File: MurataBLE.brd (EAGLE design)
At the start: 90 x 70 mm, 52 parts, among them IC1 I-5448, X1 TSW-114-02-S-S, X2 TSW-114-02-S-S

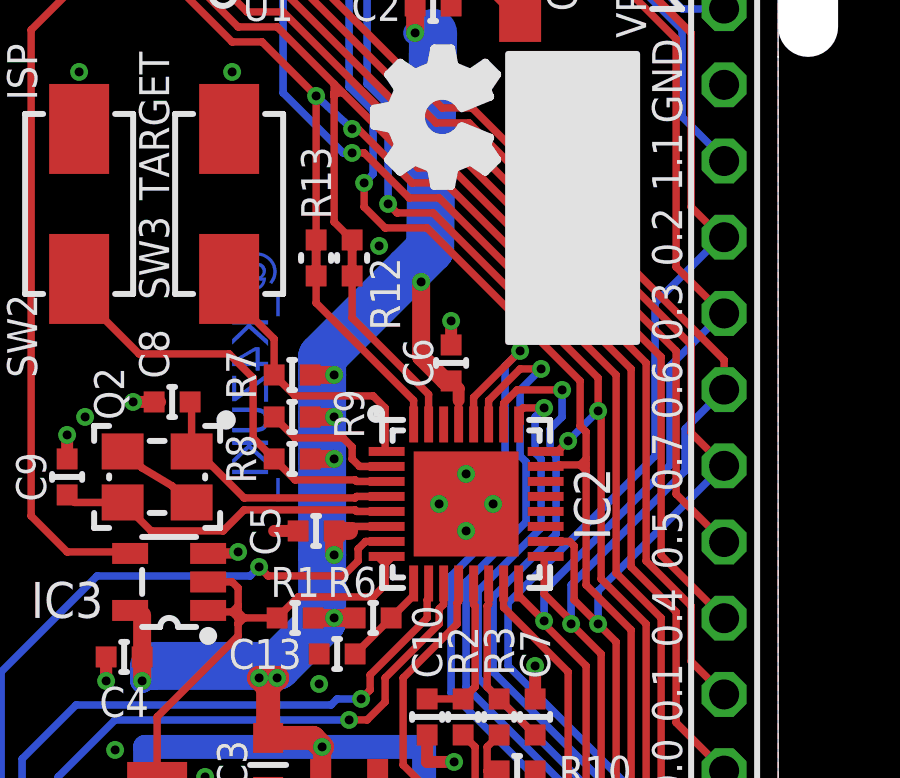
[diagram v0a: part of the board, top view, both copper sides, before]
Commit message: [ USB ] add SWD pulp R14/15
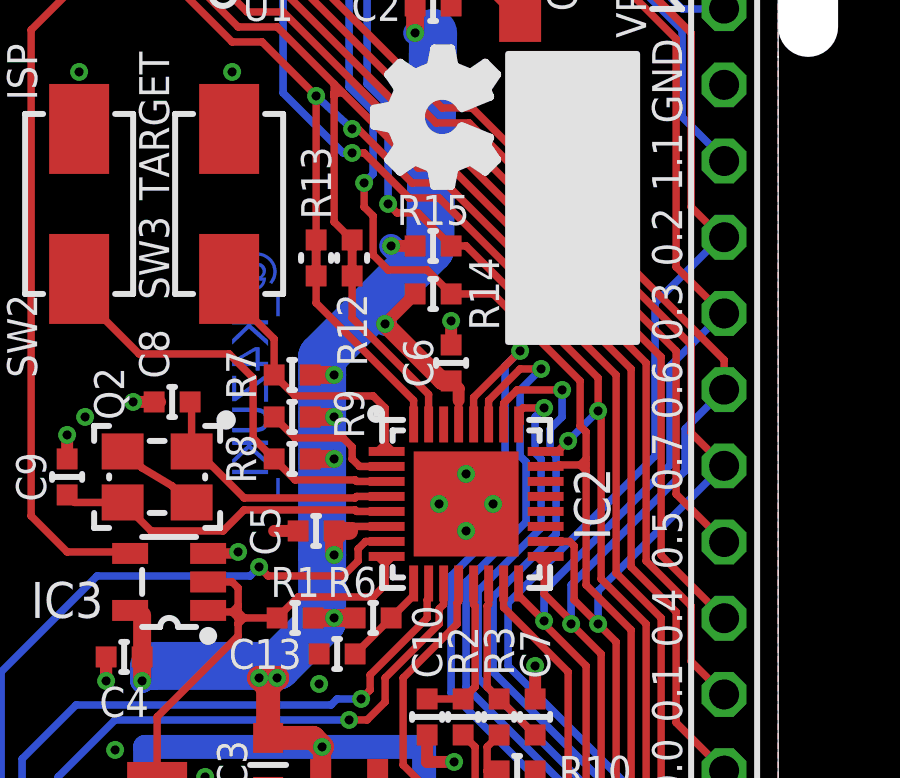
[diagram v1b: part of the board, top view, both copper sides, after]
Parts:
- added R14, R15: 10k/1005, mylib:C0402
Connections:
- net 3.3V: now also R14.2, R15.2
- net SWCLK: now also R14.1
- net SWDIO: now also R15.1
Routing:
- net 3.3V: track 96.3 -> 98.8 mm, vias 12 -> 13
- net SWCLK: track 42.9 -> 43.6 mm
- net FB_BL: track 9.45 -> 10.0 mm
- net 580.P0_6: track 52.0 -> 52.6 mm
- net GND: vias 71 -> 70
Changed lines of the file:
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@@
 <element name="R12" library="mylib" package="R0402SHORT" value="" x="24.8" y="43.2" smashed="yes" rot="R90">
 <attribute name="NOT_COMPONENT" value="YES" x="24.8" y="43.2" size="1.778" layer="27" rot="R90" display="off"/>
-<attribute name="NAME" x="25.9" y="42" size="1" layer="25" font="vector" ratio="20" rot="R90" align="center"/>
+<attribute name="NAME" x="24.8" y="40.8" size="1" layer="25" font="vector" ratio="20" rot="R90" align="center"/>
 <attribute name="VALUE" x="24.8" y="43.2" size="1" layer="27" font="vector" rot="R90" align="center"/>
 </element>
@@
 <attribute name="MOUSER" value="" x="11.8" y="35" size="1.778" layer="27" rot="R270" display="off"/>
 <attribute name="DIGIKEY" value="" x="11.8" y="35" size="1.778" layer="27" rot="R270" display="off"/>
+</element>
+<element name="R14" library="mylib" package="C0402" value="10k/1005" x="27.5" y="42" smashed="yes" rot="R180">
+<attribute name="MOUSER" value="" x="27.5" y="42" size="1.778" layer="27" rot="R180" display="off"/>
+<attribute name="AKIZUKI" value="" x="27.5" y="42" size="1.778" layer="27" rot="R180" display="off"/>
+<attribute name="DIGIKEY" value="P10.0KLCT-ND" x="27.5" y="42" size="1.778" layer="27" rot="R180" display="off"/>
+<attribute name="SEEED" value="301010047 " x="27.5" y="42" size="1.778" layer="27" rot="R180" display="off"/>
+<attribute name="NAME" x="29.2" y="42" size="1" layer="25" font="vector" ratio="20" rot="R270" align="center"/>
+<attribute name="VALUE" x="27.5" y="42" size="1" layer="27" font="vector" rot="R180" align="center"/>
+</element>
+<element name="R15" library="mylib" package="C0402" value="10k/1005" x="27.5" y="43.6" smashed="yes" rot="R180">
+<attribute name="MOUSER" value="" x="27.5" y="43.6" size="1.778" layer="27" rot="R180" display="off"/>
+<attribute name="AKIZUKI" value="" x="27.5" y="43.6" size="1.778" layer="27" rot="R180" display="off"/>
+<attribute name="DIGIKEY" value="P10.0KLCT-ND" x="27.5" y="43.6" size="1.778" layer="27" rot="R180" display="off"/>
+<attribute name="SEEED" value="301010047 " x="27.5" y="43.6" size="1.778" layer="27" rot="R180" display="off"/>
+<attribute name="NAME" x="27.5" y="44.8" size="1" layer="25" font="vector" ratio="20" rot="R180" align="center"/>
+<attribute name="VALUE" x="27.5" y="43.6" size="1" layer="27" font="vector" rot="R180" align="center"/>
 </element>
 </elements>
@@
 <contactref element="IC2" pad="EXP"/>
 <wire x1="29.5" y1="35" x2="28.6" y2="35" width="0.25" layer="1"/>
-<via x="25.7" y="43.6" extent="1-16" drill="0.3" diameter="0.45"/>
 <contactref element="C11" pad="2"/>
 <contactref element="C12" pad="2"/>
@@
 <wire x1="23.8" y1="37.9" x2="24.2" y2="37.9" width="0.8" layer="16"/>
 <wire x1="27.4" y1="43.5" x2="27.5" y2="50.7" width="1.6" layer="16"/>
-<wire x1="28.1" y1="39.1" x2="27.9" y2="39.1" width="0.6" layer="1"/>
-<wire x1="27.9" y1="39.1" x2="27.1" y2="39.9" width="0.6" layer="1"/>
+<wire x1="28.1" y1="39.1" x2="27.8" y2="39.1" width="0.6" layer="1"/>
+<wire x1="27.8" y1="39.1" x2="25.9" y2="41" width="0.6" layer="1"/>
 <wire x1="25.95" y1="34.25" x2="24.85" y2="34.25" width="0.25" layer="1"/>
 <wire x1="24.85" y1="34.25" x2="24.8" y2="34.2" width="0.25" layer="1"/>
@@
 <wire x1="29.8" y1="25.4" x2="27.2" y2="25.4" width="0.25" layer="16"/>
 <wire x1="23.8" y1="39.3" x2="23.8" y2="39.9" width="1.6" layer="16"/>
-<wire x1="23.8" y1="39.9" x2="26.7" y2="42.8" width="1.6" layer="16"/>
-<wire x1="26.7" y1="42.8" x2="27.4" y2="43.5" width="1.6" layer="16"/>
-<wire x1="27.1" y1="42.4" x2="27.1" y2="39.9" width="0.6" layer="1"/>
+<wire x1="23.8" y1="39.9" x2="25.4" y2="41.5" width="1.6" layer="16"/>
+<wire x1="25.4" y1="41.5" x2="26.8" y2="42.9" width="1.6" layer="16"/>
 <contactref element="IC3" pad="5"/>
+<wire x1="26.8" y1="42.9" x2="27.4" y2="43.5" width="1.6" layer="16"/>
 <wire x1="17.8" y1="31.45" x2="17.4" y2="31.45" width="0.25" layer="1"/>
 <wire x1="28.35" y1="38.45" x2="28.35" y2="38.85" width="0.4" layer="1"/>
 <wire x1="28.35" y1="38.85" x2="28.1" y2="39.1" width="0.4" layer="1"/>
-<via x="27.1" y="42.4" extent="1-16" drill="0.3"/>
-<wire x1="27.1" y1="42.4" x2="26.7" y2="42.8" width="0.6" layer="16"/>
+<via x="25.9" y="41" extent="1-16" drill="0.3"/>
+<wire x1="25.9" y1="41" x2="25.4" y2="41.5" width="0.8" layer="16"/>
 <wire x1="21.7" y1="29.6" x2="21.7" y2="29.2" width="0.8" layer="16"/>
 <wire x1="22.3" y1="29.6" x2="22.3" y2="29.2" width="0.8" layer="16"/>
 <via x="21.7" y="29.2" extent="1-16" drill="0.3"/>
 <via x="22.3" y="29.2" extent="1-16" drill="0.3"/>
+<contactref element="R14" pad="2"/>
+<contactref element="R15" pad="2"/>
+<wire x1="25.9" y1="41" x2="26.9" y2="42" width="0.4" layer="1"/>
+<wire x1="26.9" y1="43.6" x2="26.1" y2="43.6" width="0.4" layer="1"/>
+<via x="26.1" y="43.6" extent="1-16" drill="0.3"/>
+<wire x1="26.1" y1="43.6" x2="26.8" y2="42.9" width="0.8" layer="16"/>
 </signal>
 <signal name="RESET">
@@
 <contactref element="IC5" pad="6"/>
 <wire x1="31.25" y1="33.25" x2="31.2" y2="33.2" width="0.25" layer="1"/>
-<wire x1="31.2" y1="33.2" x2="31.2" y2="32" width="0.25" layer="1"/>
+<wire x1="31.2" y1="33.2" x2="31.2" y2="33" width="0.25" layer="1"/>
 <via x="32.1" y="31" extent="1-16" drill="0.3"/>
+<wire x1="31.2" y1="33" x2="31.2" y2="32" width="0.25" layer="1"/>
 <wire x1="32.1" y1="31" x2="33.1" y2="30" width="0.25" layer="1"/>
 <wire x1="33.1" y1="30" x2="33.1" y2="24.5" width="0.25" layer="1"/>
@@
 <wire x1="32.1" y1="31" x2="32.1" y2="31.1" width="0.25" layer="1"/>
 <wire x1="32.1" y1="31.1" x2="31.2" y2="32" width="0.25" layer="1"/>
+<wire x1="31.2" y1="33" x2="31" y2="33.2" width="0.25" layer="1"/>
+<wire x1="31.2" y1="33" x2="31.4" y2="33.2" width="0.25" layer="1"/>
 </signal>
 <signal name="580.P0_7">
@@
 <wire x1="32.6" y1="36.3" x2="32.6" y2="36.5" width="0.25" layer="1"/>
 <wire x1="32.6" y1="36.5" x2="32.6" y2="37.4" width="0.25" layer="1"/>
-<wire x1="32.4" y1="39.1" x2="27.3" y2="44.2" width="0.25" layer="1"/>
-<wire x1="27.3" y1="44.2" x2="25.9" y2="44.2" width="0.25" layer="1"/>
+<wire x1="32.4" y1="39.1" x2="29.5" y2="42" width="0.25" layer="1"/>
 <wire x1="25.2" y1="45.7" x2="25.2" y2="44.9" width="0.25" layer="1"/>
-<wire x1="25.2" y1="44.9" x2="25.9" y2="44.2" width="0.25" layer="1"/>
+<wire x1="25.2" y1="44.9" x2="25.5" y2="44.6" width="0.25" layer="1"/>
 <contactref element="IC2" pad="23"/>
 <wire x1="31.25" y1="36.25" x2="31.65" y2="36.25" width="0.25" layer="1"/>
@@
 <wire x1="32.4" y1="39.1" x2="32.4" y2="37.6" width="0.25" layer="1"/>
 <wire x1="32.4" y1="37.6" x2="32.6" y2="37.4" width="0.25" layer="1"/>
+<contactref element="R14" pad="1"/>
+<wire x1="29.5" y1="42" x2="28.1" y2="42" width="0.25" layer="1"/>
+<wire x1="28.1" y1="42" x2="27.3" y2="42.8" width="0.25" layer="1"/>
+<wire x1="25.5" y1="43.3" x2="26" y2="42.8" width="0.25" layer="1"/>
+<wire x1="25.5" y1="44.6" x2="25.5" y2="43.3" width="0.25" layer="1"/>
+<wire x1="26" y1="42.8" x2="27.3" y2="42.8" width="0.25" layer="1"/>
 </signal>
 <signal name="N$18">
@@
 <contactref element="SW3" pad="2"/>
 <contactref element="R7" pad="2"/>
-<wire x1="25.9" y1="38.2" x2="25.9" y2="36.8" width="0.25" layer="1"/>
+<wire x1="25.9" y1="38.2" x2="25.9" y2="37" width="0.25" layer="1"/>
+<wire x1="25.9" y1="37" x2="25.9" y2="36.8" width="0.25" layer="1"/>
 <wire x1="25.95" y1="36.75" x2="25.9" y2="36.8" width="0.25" layer="1"/>
 <wire x1="22.2" y1="39.3" x2="22.9" y2="38.6" width="0.25" layer="1"/>
@@
 <wire x1="20.7" y1="42" x2="20.7" y2="42.5" width="0.25" layer="1"/>
 <contactref element="IC2" pad="1"/>
+<wire x1="25.9" y1="37" x2="25.7" y2="36.8" width="0.25" layer="1"/>
+<wire x1="25.9" y1="37" x2="26.1" y2="36.8" width="0.25" layer="1"/>
 </signal>
 <signal name="FB_ISP">
@@
 <wire x1="33.1" y1="38" x2="33" y2="38.1" width="0.25" layer="1"/>
 <wire x1="33" y1="38.1" x2="33" y2="39.2" width="0.25" layer="1"/>
-<wire x1="33" y1="39.2" x2="27.5" y2="44.7" width="0.25" layer="1"/>
-<wire x1="27.5" y1="44.7" x2="26.3" y2="44.7" width="0.25" layer="1"/>
+<wire x1="33" y1="39.2" x2="28.6" y2="43.6" width="0.25" layer="1"/>
+<wire x1="27" y1="44.7" x2="26.3" y2="44.7" width="0.25" layer="1"/>
 <wire x1="26.3" y1="44.7" x2="26" y2="45" width="0.25" layer="1"/>
 <contactref element="IC2" pad="24"/>
@@
 <via x="33" y="38.1" extent="1-16" drill="0.3"/>
 <wire x1="32" y1="37.1" x2="33" y2="38.1" width="0.25" layer="16"/>
+<contactref element="R15" pad="1"/>
+<wire x1="28.1" y1="43.6" x2="28.6" y2="43.6" width="0.25" layer="1"/>
+<wire x1="28.1" y1="43.6" x2="27" y2="44.7" width="0.25" layer="1"/>
 </signal>
 <signal name="580.P0_0">

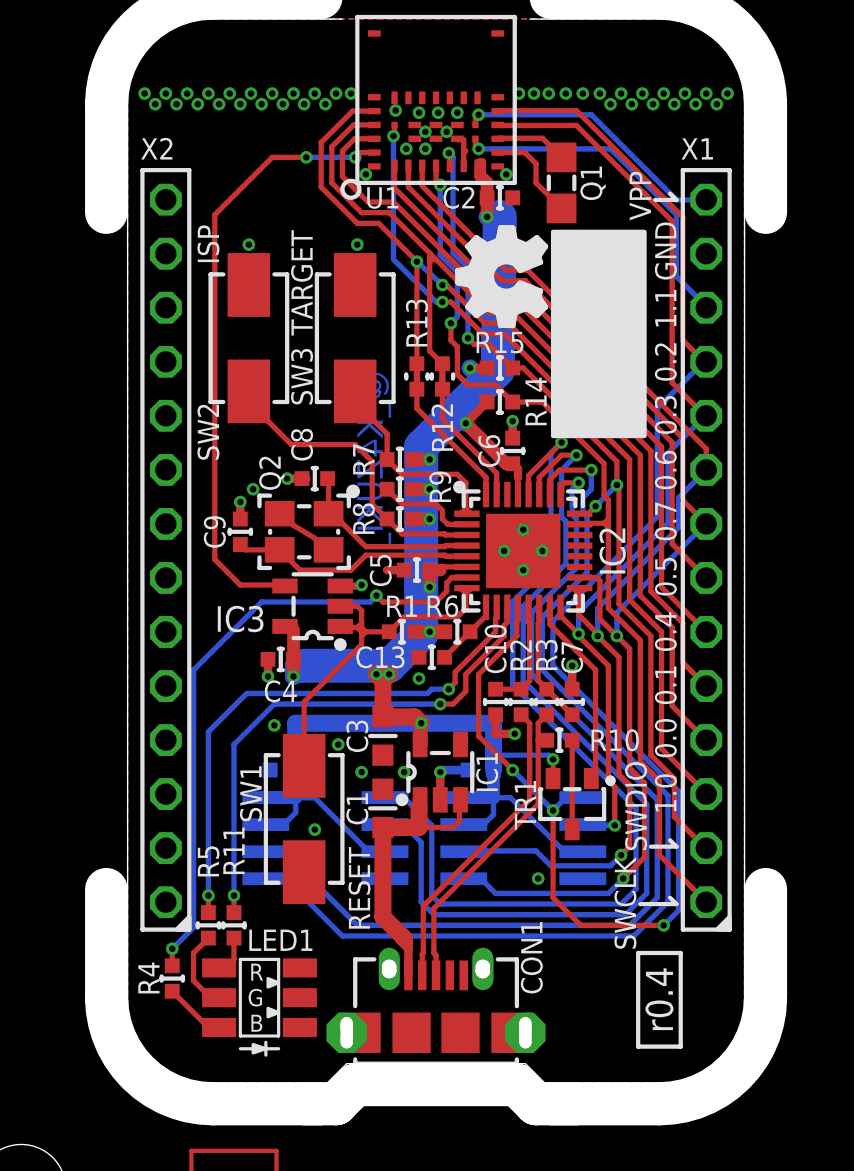
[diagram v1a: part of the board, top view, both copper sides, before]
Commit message: [ USB ]add values; panelized
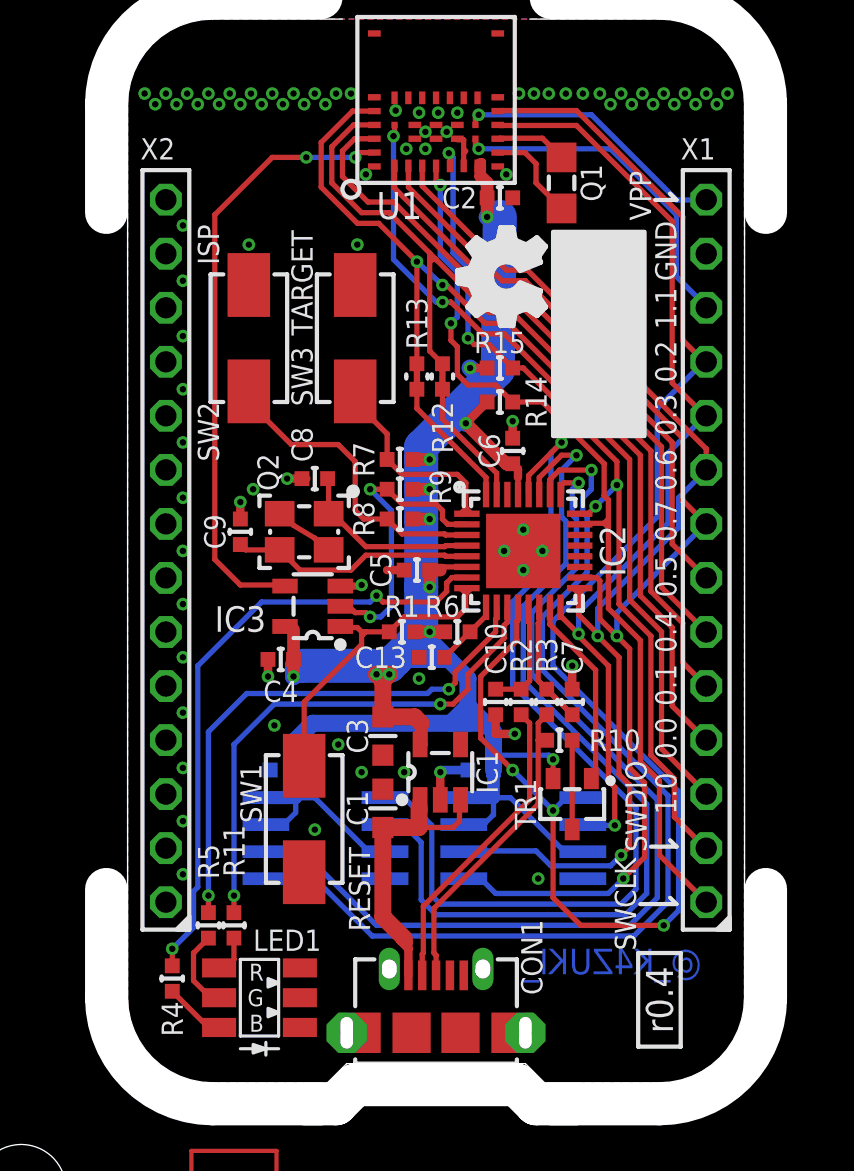
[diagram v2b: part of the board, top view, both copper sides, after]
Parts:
- CON1: value (none) -> 47589-0001
- GIT1: value (none) -> 688904b
- IC2: value (none) -> LPC11U35_QFN33
- IC3: value (none) -> NC7SZ00
- IC4: value (none) -> AT25DN512C
- IC5: value (none) -> AT25XE011
- ICON2, P1, P2, P3, P4, R12, R13: value (none) -> NC
- Q1: value (none) -> 32.768K/2012
- Q2: value (none) -> 12M/3225
- R11, R4, R5: value (none) -> 1k/1005
- SW1, SW2, SW3: value (none) -> FSM2JMTR
- TP100, TP101, TP102: value TESTPAD_F -> NC
- TR1: value PMOS_BSS84_SOT23 -> BSS84
- U1: value (none) -> LBCA2HNZYZ
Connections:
- net !RESET!: no longer IC3.2
- net N$5: now also IC3.2
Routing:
- net N$5: track 4.67 -> 14.2 mm, vias 0 -> 2
- net 3.3V: track 98.8 -> 107.9 mm, vias 13 -> 12
- net !RESET!: track 18.5 -> 15.7 mm
- net GND: vias 70 -> 83
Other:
- board text added: "C1"
- board text added: "C10"
- board text added: "C11"
- board text added: "C12"
- board text added: "C13"
- board text added: "C2"
- board text added: "C3"
- board text added: "C4"
- board text added: "C5"
- board text added: "C6"
- board text added: "C7"
- board text added: "C8"
- board text added: "C9"
- board text added: "CON1"
- board text added: "IC1"
- board text added: "IC2"
- board text added: "IC3"
- board text added: "IC4"
- board text added: "IC5"
- board text added: "LED1"
- board text added: "Q1"
- board text added: "Q2"
- board text added: "R1"
- board text added: "R10"
- board text added: "R11"
- board text added: "R12"
- board text added: "R13"
- board text added: "R14"
- board text added: "R15"
- board text added: "R2"
- board text added: "R3"
- board text added: "R4"
- board text added: "R5"
- board text added: "R6"
- board text added: "R7"
- board text added: "R8"
- board text added: "R9"
- board text added: "SW1"
- board text added: "SW2"
- board text added: "SW3"
- board text added: "TR1"
- board text added: "U1"
- board text added: "X1"
- board text added: "X2"

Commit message: [ USB ] fix OpenDrain problem
P0_4 and 5 are used for I2C; has limitation of open drain
change polarity of LED1 to pull current from 3.3V line
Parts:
- turned LED1 to 0 degrees
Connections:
- net 3.3V: now also LED1.4, LED1.5, LED1.6
- net GND: no longer LED1.1, LED1.2, LED1.3
- net N$11: now also LED1.1, R11.2; no longer LED1.4, R4.2
- net N$12: now also LED1.2; no longer LED1.5
- net N$13: now also LED1.3, R4.2; no longer LED1.6, R11.2
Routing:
- net 3.3V: track 107.9 -> 126.3 mm, vias 12 -> 13
- net N$13: track 1.87 -> 2.90 mm
- net N$11: track 2.90 -> 1.87 mm
